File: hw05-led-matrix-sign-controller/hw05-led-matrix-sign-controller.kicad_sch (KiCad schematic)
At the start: 13 parts, among them J101 SameSky PJ-002A, J102 USB_B, J103 TE 640456-4, U101 ESP32-C3-WROOM-02U-N4, U102 D78B33-0.5, U103 MAX3485

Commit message: Fix footprint
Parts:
- A101: footprint Connector_PinHeader_1.00mm:PinHeader_2x05_P1.00mm_Vertical -> Connector_PinHeader_2.54mm:PinHeader_2x05_P2.54mm_Vertical
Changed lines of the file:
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@@
 			)
 		)
-		(property "Footprint" "Connector_PinHeader_1.00mm:PinHeader_2x05_P1.00mm_Vertical"
+		(property "Footprint" "Connector_PinHeader_2.54mm:PinHeader_2x05_P2.54mm_Vertical"
 			(at 197.358 9.144 0)
 			(effects

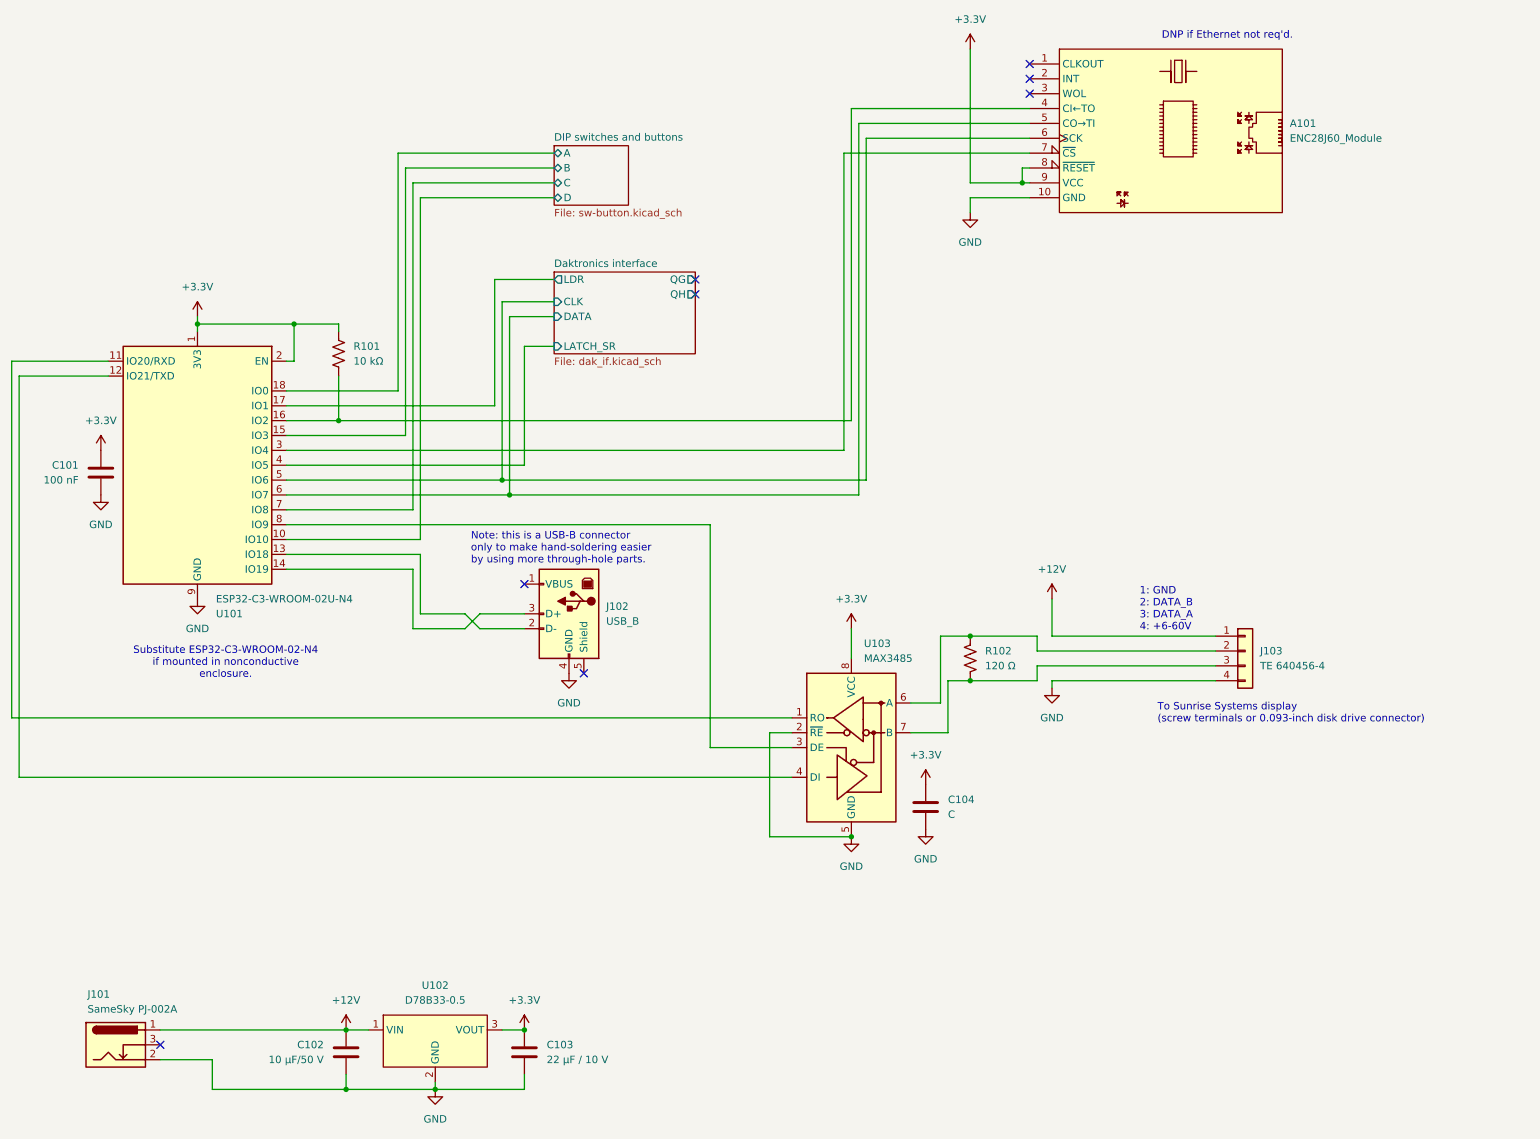
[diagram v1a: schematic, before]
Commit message: Fix pullup
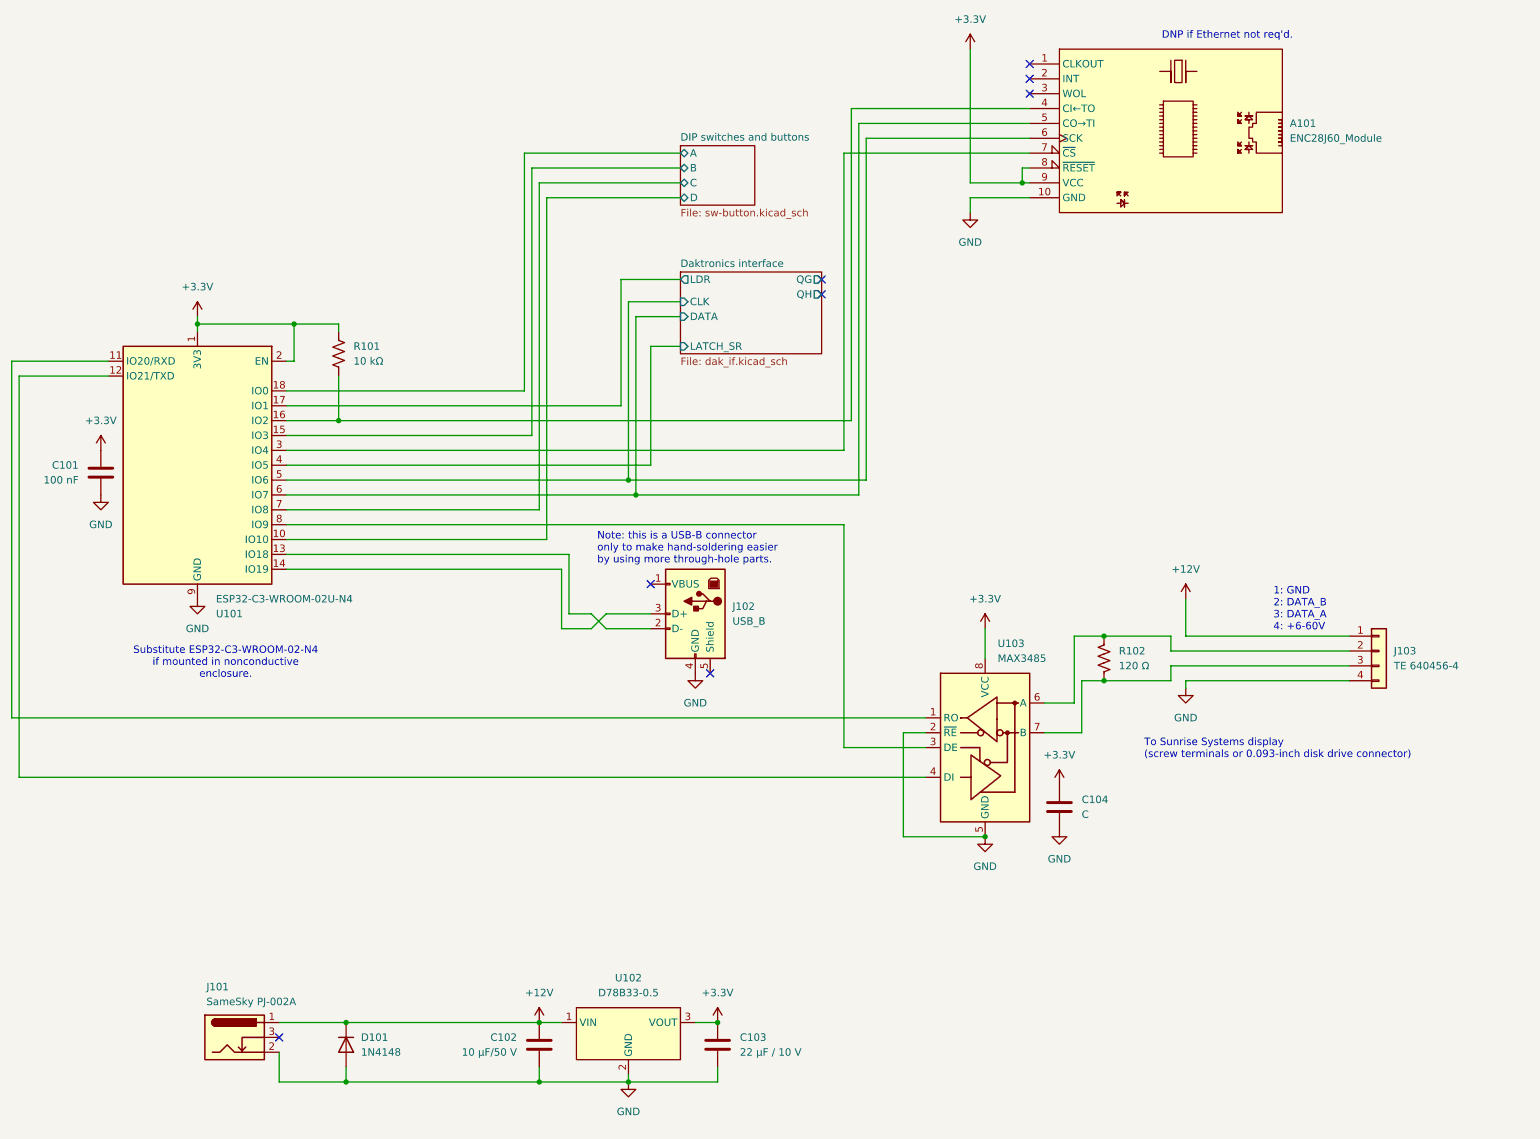
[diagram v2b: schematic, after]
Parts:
- added D101: 1N4148, Diode_THT:D_DO-35_SOD27_P7.62mm_Horizontal, symbol Diode:1N4148
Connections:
- net +12V: now also D101.1 (K)
- net GND: now also D101.2 (A)
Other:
- moved on the sheet: C102, C103, C104, J101, J102, J103, R102, U102, U103

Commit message: Add headers for future use
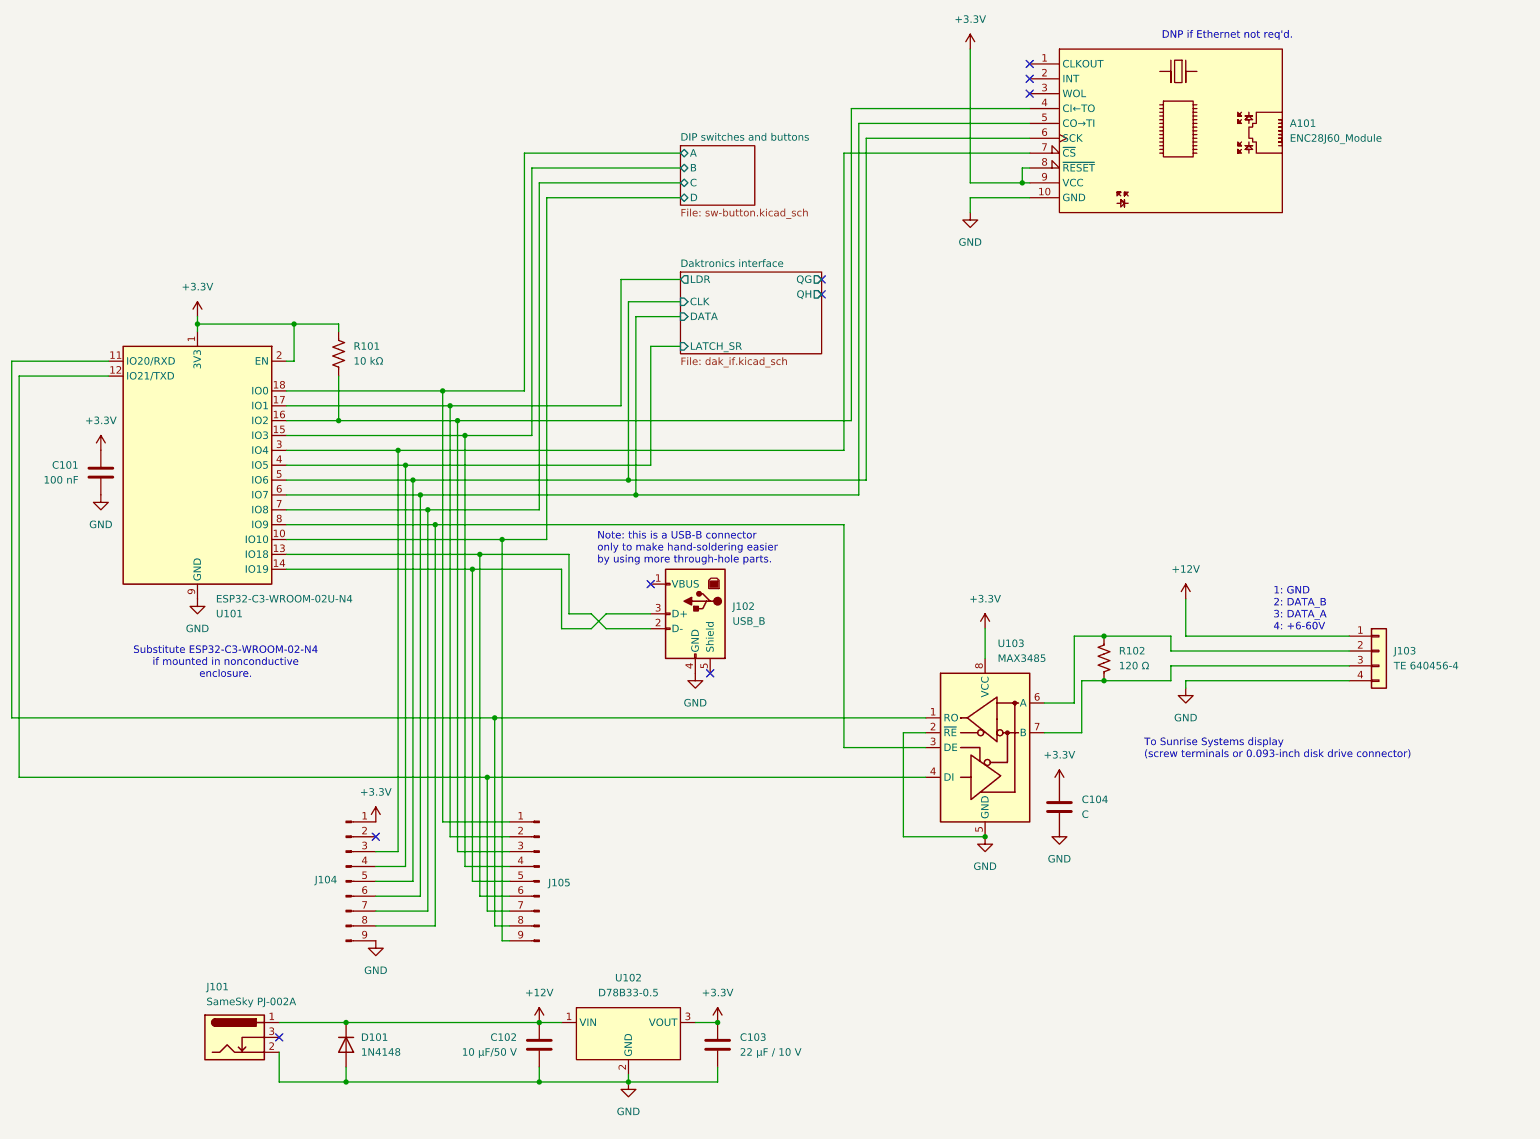
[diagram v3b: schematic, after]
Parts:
- added J104, J105: Conn_01x09_Pin, Connector_PinHeader_2.54mm:PinHeader_1x09_P2.54mm_Vertical, symbol Connector:Conn_01x09_Pin
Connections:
- net +3.3V: now also J104.1 (Pin_1)
- net DIP switches and buttons/A: now also J105.1 (Pin_1)
- net DIP switches and buttons/B: now also J105.4 (Pin_4)
- net DIP switches and buttons/C: now also J104.7 (Pin_7)
- net DIP switches and buttons/D: now also J105.9 (Pin_9)
- net Daktronics interface/CLK: now also J104.5 (Pin_5)
- net Daktronics interface/DATA: now also J104.6 (Pin_6)
- net Daktronics interface/LATCH_SR: now also J104.4 (Pin_4)
- net Daktronics interface/LDR: now also J105.2 (Pin_2)
- net GND: now also J104.9 (Pin_9)
- net at A101.4 (CI←TO), R101.2, U101.16 (IO2): now also J105.3 (Pin_3)
- net at A101.7 (~{CS}), U101.3 (IO4): now also J104.3 (Pin_3)
- net at U101.11 (IO20/RXD), U103.1 (RO): now also J105.8 (Pin_8)
- net at U101.12 (IO21/TXD), U103.4 (DI): now also J105.7 (Pin_7)
- net at J102.2 (D-), U101.13 (IO18): now also J105.6 (Pin_6)
- net at J102.3 (D+), U101.14 (IO19): now also J105.5 (Pin_5)
- net at U101.8 (IO9), U103.3 (DE): now also J104.8 (Pin_8)
- no-connect marks 8 -> 9
